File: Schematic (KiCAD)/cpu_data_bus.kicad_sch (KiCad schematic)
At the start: 144 parts, among them P13 INVERT, P19 INVERT, P26 INVERT, P5 INVERT, P7 INVERT, X18 INVERT, X19 INVERT, X20 INVERT, X21 INVERT, X22 INVERT, X23 INVERT, X24 INVERT, X25 INVERT, Y11 INVERT, Y12 INVERT, Y18 INVERT, Y19 INVERT, Y25 INVERT, Y26 INVERT, Y4 INVERT, Y5 INVERT

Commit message: - Started work on the pulse channels.  - Solved at least 2 of the red traces in the SVG.  - Finally realized that "Unknown 4to1" cells are actually just ordinary And-Or-Invert "AOI22" cells.
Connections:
- net at BK47. (X): now also BK46. (X); no longer BL50. (X)
- net at BK51. (X): now also BK49. (X); no longer BK52. (X)
- new net: BK55. (X), BK56. (X), BK61. (X), BK62. (X), BK67. (X), BK68. (X), BK73. (X), BK74. (X), BL58. (X)
- new net: BK55. (X), BK56. (X), BK61. (X), BK62. (X), BK67. (X), BK68. (X), BK73. (X), BK74. (X), BL59. (X)
- new net: BK66. (X), BK67. (X)
- new net: BK53. (X), BK58. (X), BK59. (X), BK64. (X), BK65. (X), BK70. (X), BK71. (X), BK76. (X), BL61. (X)
- new net: BK63. (X), BK64. (X)
- new net: BK69. (X), BK70. (X)
- new net: BK68. (X), BK69. (X)
- new net: BK65. (X), BK66. (X)
- new net: BK57. (X), BK58. (X)
- new net: G15. (X), G16. (X)
- new net: BK75. (X), BK76. (X)
- new net: G10. (X), G9. (X)
- new net: AE13. (X), AE19. (X), G13. (X), MUL20. (X), X19. (X)
- new net: BK47. (X), BL50. (X)
- new net: G1. (X), G2. (X)
- new net: G7. (X), G8. (X)
- new net: G11. (X), G12. (X)
- new net: G5. (X), G6. (X)
- new net: BK53. (X), BK54. (X)
- new net: G3. (X), G4. (X)
- new net: BK48. (X), BP2. (X)
- new net: BP2. (X), BP3. (X)
- new net: BK55. (X), BK73. (X), BK74. (X), BL60. (X)
- new net: BK54. (X), BK55. (X)
- new net: BK72. (X), BK73. (X)
- new net: BK71. (X), BK72. (X)
- new net: BK74. (X), BK75. (X)
- new net: BK74. (X), BL57. (X)
- new net: B26. (X), B27. (X)
- new net: BK60. (X), BK61. (X)
- new net: BK59. (X), BK60. (X)
- new net: BK56. (X), BK57. (X)
- new net: BK62. (X), BK63. (X)
- new net: BK51. (X), BK52. (X)
- new net: BP1. (X), BP2. (X)
- new net: BK50. (X), BK51. (X)
- new net: BK46. (X), BK51. (X)
- new net: BP2. (X), BP4. (X)
- new net: BK45. (X), BK46. (X)

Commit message: - Pulse DAC logic is now complete.  - The 4-bit adders are verified correct using Excel.    - This revealed 1 tracing error and also 3 XNOR gates that are actually XOR in this case.  - Now including a PDF version of the schematic.
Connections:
- net at BK47. (X): now also BK46. (X); no longer BL50. (X)
- net at BK51. (X): now also BK49. (X); no longer BK52. (X)
- new net: BK55. (X), BK56. (X), BK61. (X), BK62. (X), BK67. (X), BK68. (X), BK73. (X), BK74. (X), BL58. (X)
- new net: BK55. (X), BK56. (X), BK61. (X), BK62. (X), BK67. (X), BK68. (X), BK73. (X), BK74. (X), BL59. (X)
- new net: BK66. (X), BK67. (X)
- new net: BK53. (X), BK58. (X), BK59. (X), BK64. (X), BK65. (X), BK70. (X), BK71. (X), BK76. (X), BL61. (X)
- new net: BK63. (X), BK64. (X)
- new net: BK69. (X), BK70. (X)
- new net: BK68. (X), BK69. (X)
- new net: BK65. (X), BK66. (X)
- new net: BK57. (X), BK58. (X)
- new net: G15. (X), G16. (X)
- new net: BK75. (X), BK76. (X)
- new net: G10. (X), G9. (X)
- new net: AE13. (X), AE19. (X), G13. (X), MUL20. (X), X19. (X)
- new net: BK47. (X), BL50. (X)
- new net: G1. (X), G2. (X)
- new net: G7. (X), G8. (X)
- new net: G11. (X), G12. (X)
- new net: G5. (X), G6. (X)
- new net: BK53. (X), BK54. (X)
- new net: G3. (X), G4. (X)
- new net: BK48. (X), BP2. (X)
- new net: BP2. (X), BP3. (X)
- new net: BK55. (X), BK73. (X), BK74. (X), BL60. (X)
- new net: BK54. (X), BK55. (X)
- new net: BK72. (X), BK73. (X)
- new net: BK71. (X), BK72. (X)
- new net: BK74. (X), BK75. (X)
- new net: BK74. (X), BL57. (X)
- new net: B26. (X), B27. (X)
- new net: BK60. (X), BK61. (X)
- new net: BK59. (X), BK60. (X)
- new net: BK56. (X), BK57. (X)
- new net: BK62. (X), BK63. (X)
- new net: BK51. (X), BK52. (X)
- new net: BP1. (X), BP2. (X)
- new net: BK50. (X), BK51. (X)
- new net: BK46. (X), BK51. (X)
- new net: BP2. (X), BP4. (X)
- new net: BK45. (X), BK46. (X)

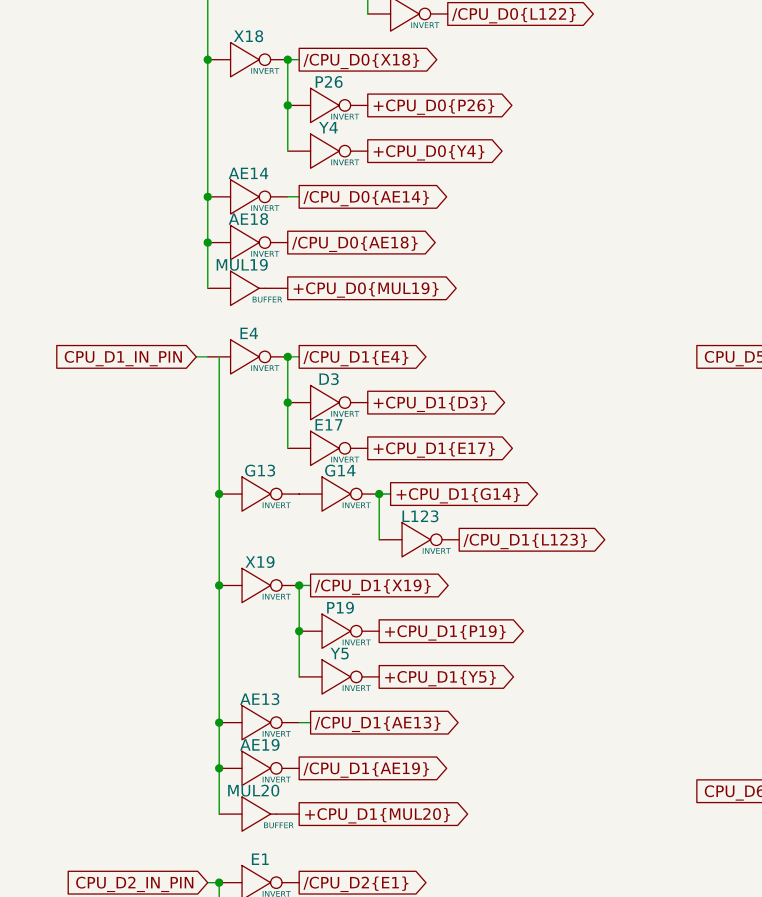
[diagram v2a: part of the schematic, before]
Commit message: Schematic Updates:  - Added all 10-bit CHR banking registers $5120 - $512B, including where all 10 bits come from when written.  - Added 8-bit CHR bank register $5202, which is the bank used when rendering the V-Split region.    + V-Split seems to always be 8-bit, 8kB bank regardless of CHR mode.  The wiki doesn't say that and I don't know for sure.  - Added decoding logic that activates the correct CHR bank for CHR A10, A11, A12 (corresponding to columns AV, AW, AX).  - Noted, AX15 activates $5202 CHR Bank for V-Split region.  AX16 activates CHR Bank from data stored in ExRAM for extended attributes.  Therefore, AX15 driven by AT1 High means we specifically are in v-split region, and not extended attribute mode.  With this knowledge, backtracking up the chain from AT1 to N14 sheds very useful insight what the 3-bit shift register at N11/N12/N13 is doing.  We now know that N14 goes low specifically for pattern table fetches when rendering the V-split region, and does not appear dual-purposed for extended attribute fetch sequencing.  This may seem rather subtle or unimportant, but it is a good advancement for higher level understanding what that mysterious shift register might be doing.
SVG Trace Updates:
 - Registers $5120, 5121, 5122, 5123 (first 4 CHR bank register), the outputs were labeled in reverse order.
 - Register $5130 (highest CHR bank bits), the outputs were labeled with backwards polarity.  The error was not having taken into account that the CPU data bus input to the latches came already inverted to begin with.
 - Still wrong: Cell AV7, 2-input NAND gate.  One of the inputs is missing and it logically should be driven by AS19 like the 4 cells to its direct right.  I can't quite make out how it makes that connection.
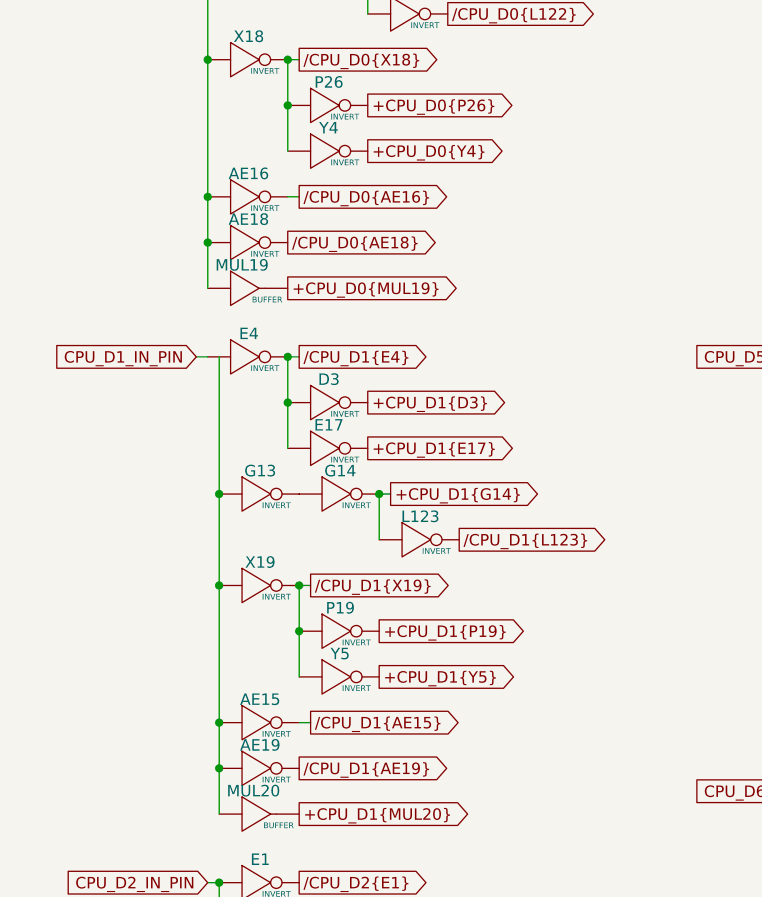
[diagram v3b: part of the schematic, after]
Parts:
- renumbered AE13 to AE15, AE14 to AE16
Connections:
- net at BK47. (X): now also BK46. (X); no longer BL50. (X)
- net at BK51. (X): now also BK49. (X); no longer BK52. (X)
- net /CPU_D0{AE14} renamed /CPU_D0{AE16}
- net /CPU_D1{AE13} renamed /CPU_D1{AE15}
- new net: BK55. (X), BK56. (X), BK61. (X), BK62. (X), BK67. (X), BK68. (X), BK73. (X), BK74. (X), BL58. (X)
- new net: BK55. (X), BK56. (X), BK61. (X), BK62. (X), BK67. (X), BK68. (X), BK73. (X), BK74. (X), BL59. (X)
- new net: BK66. (X), BK67. (X)
- new net: BK53. (X), BK58. (X), BK59. (X), BK64. (X), BK65. (X), BK70. (X), BK71. (X), BK76. (X), BL61. (X)
- new net: BK63. (X), BK64. (X)
- new net: BK69. (X), BK70. (X)
- new net: BK68. (X), BK69. (X)
- new net: BK65. (X), BK66. (X)
- new net: BK57. (X), BK58. (X)
- new net: G15. (X), G16. (X)
- new net: BK75. (X), BK76. (X)
- new net: G10. (X), G9. (X)
- new net: AE15. (X), AE19. (X), G13. (X), MUL20. (X), X19. (X)
- new net: BK47. (X), BL50. (X)
- new net: G1. (X), G2. (X)
- new net: G7. (X), G8. (X)
- new net: G11. (X), G12. (X)
- new net: G5. (X), G6. (X)
- new net: BK53. (X), BK54. (X)
- new net: G3. (X), G4. (X)
- new net: BK48. (X), BP2. (X)
- new net: BP2. (X), BP3. (X)
- new net: BK55. (X), BK73. (X), BK74. (X), BL60. (X)
- new net: BK54. (X), BK55. (X)
- new net: BK72. (X), BK73. (X)
- new net: BK71. (X), BK72. (X)
- new net: BK74. (X), BK75. (X)
- new net: BK74. (X), BL57. (X)
- new net: B26. (X), B27. (X)
- new net: BK60. (X), BK61. (X)
- new net: BK59. (X), BK60. (X)
- new net: BK56. (X), BK57. (X)
- new net: BK62. (X), BK63. (X)
- new net: BK51. (X), BK52. (X)
- new net: BP1. (X), BP2. (X)
- new net: BK50. (X), BK51. (X)
- new net: BK46. (X), BK51. (X)
- new net: BP2. (X), BP4. (X)
- new net: BK45. (X), BK46. (X)
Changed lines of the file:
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@@
 		)
 	)
-	(global_label "{slash}CPU_D1{AE13}"
+	(global_label "{slash}CPU_D1{AE15}"
 		(shape output)
 		(at 44.45 125.73 0)
@@
 		)
 	)
-	(global_label "{slash}CPU_D0{AE14}"
+	(global_label "{slash}CPU_D0{AE16}"
 		(shape output)
 		(at 43.18 67.31 0)
@@
 		(dnp no)
 		(fields_autoplaced yes)
-		(property "Reference" "AE13"
+		(property "Reference" "AE15"
 			(at 38.862 122.428 0)
 			(do_not_autoplace yes)
@@
 			(project ""
 				(path "/46093bf6-f83e-4237-9ece-7350a682aff0/f8de81e6-db49-4c78-bf33-f3fdf7c2f2f8"
-					(reference "AE13")
+					(reference "AE15")
 					(unit 1)
 				)
@@
 		(dnp no)
 		(fields_autoplaced yes)
-		(property "Reference" "AE14"
+		(property "Reference" "AE16"
 			(at 37.592 64.008 0)
 			(do_not_autoplace yes)
@@
 			(project ""
 				(path "/46093bf6-f83e-4237-9ece-7350a682aff0/f8de81e6-db49-4c78-bf33-f3fdf7c2f2f8"
-					(reference "AE14")
+					(reference "AE16")
 					(unit 1)
 				)

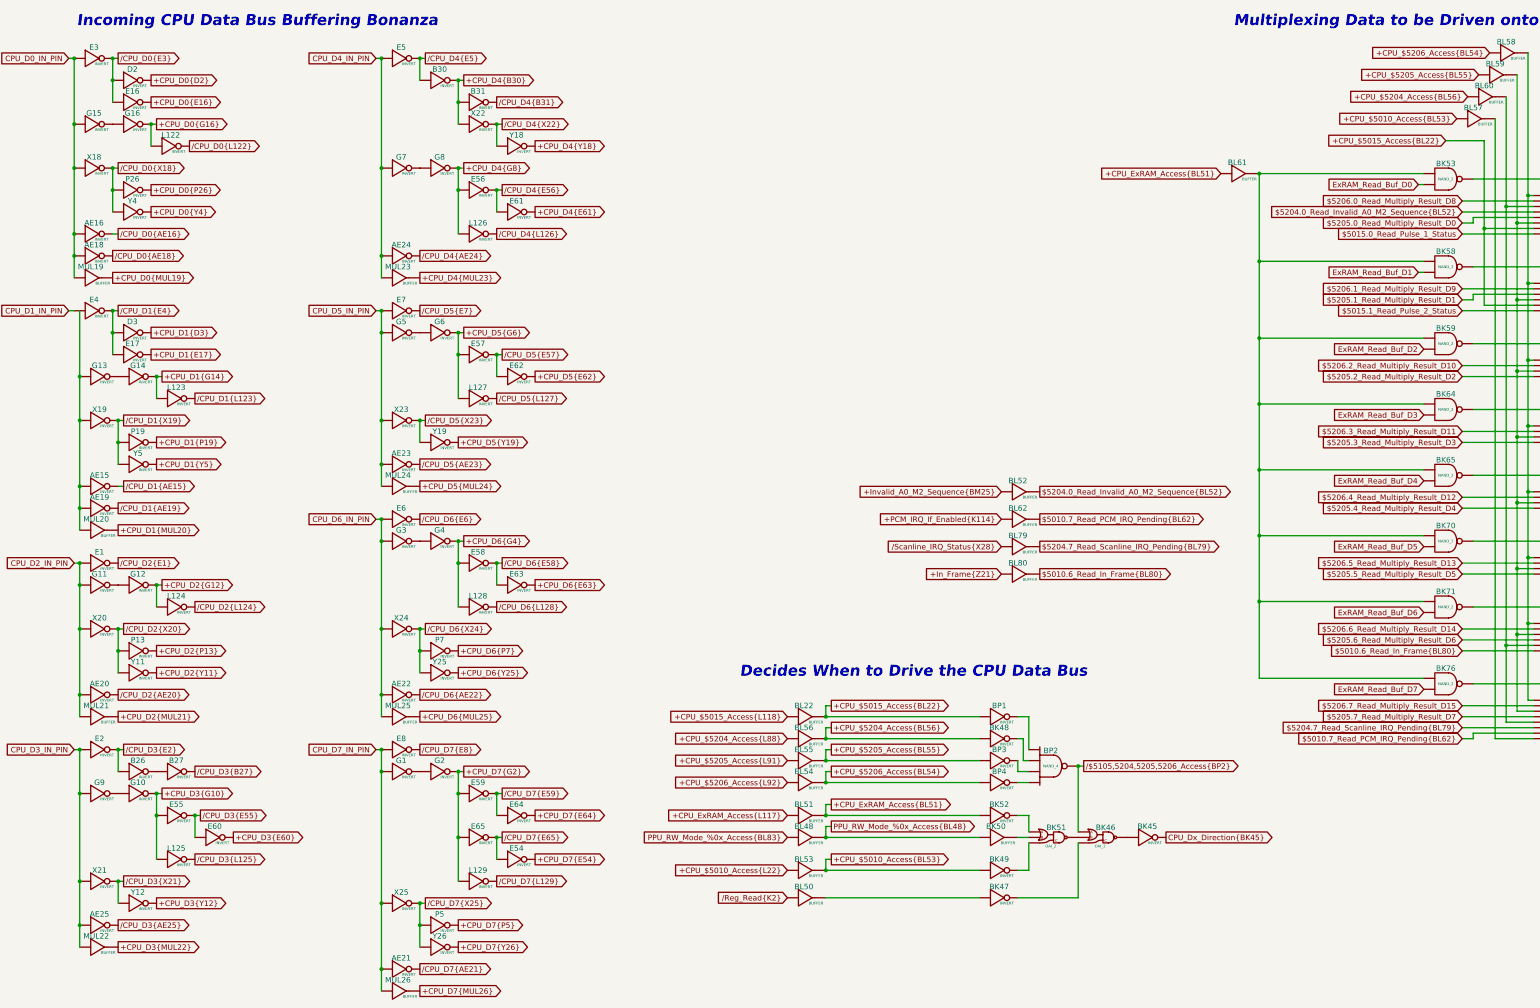
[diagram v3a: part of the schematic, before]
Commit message: - All cells in the left and center areas have now been added into the schematics.  - Changed naming of the PDF files; I was accidentally writing over furrtek's original with my new PDF.
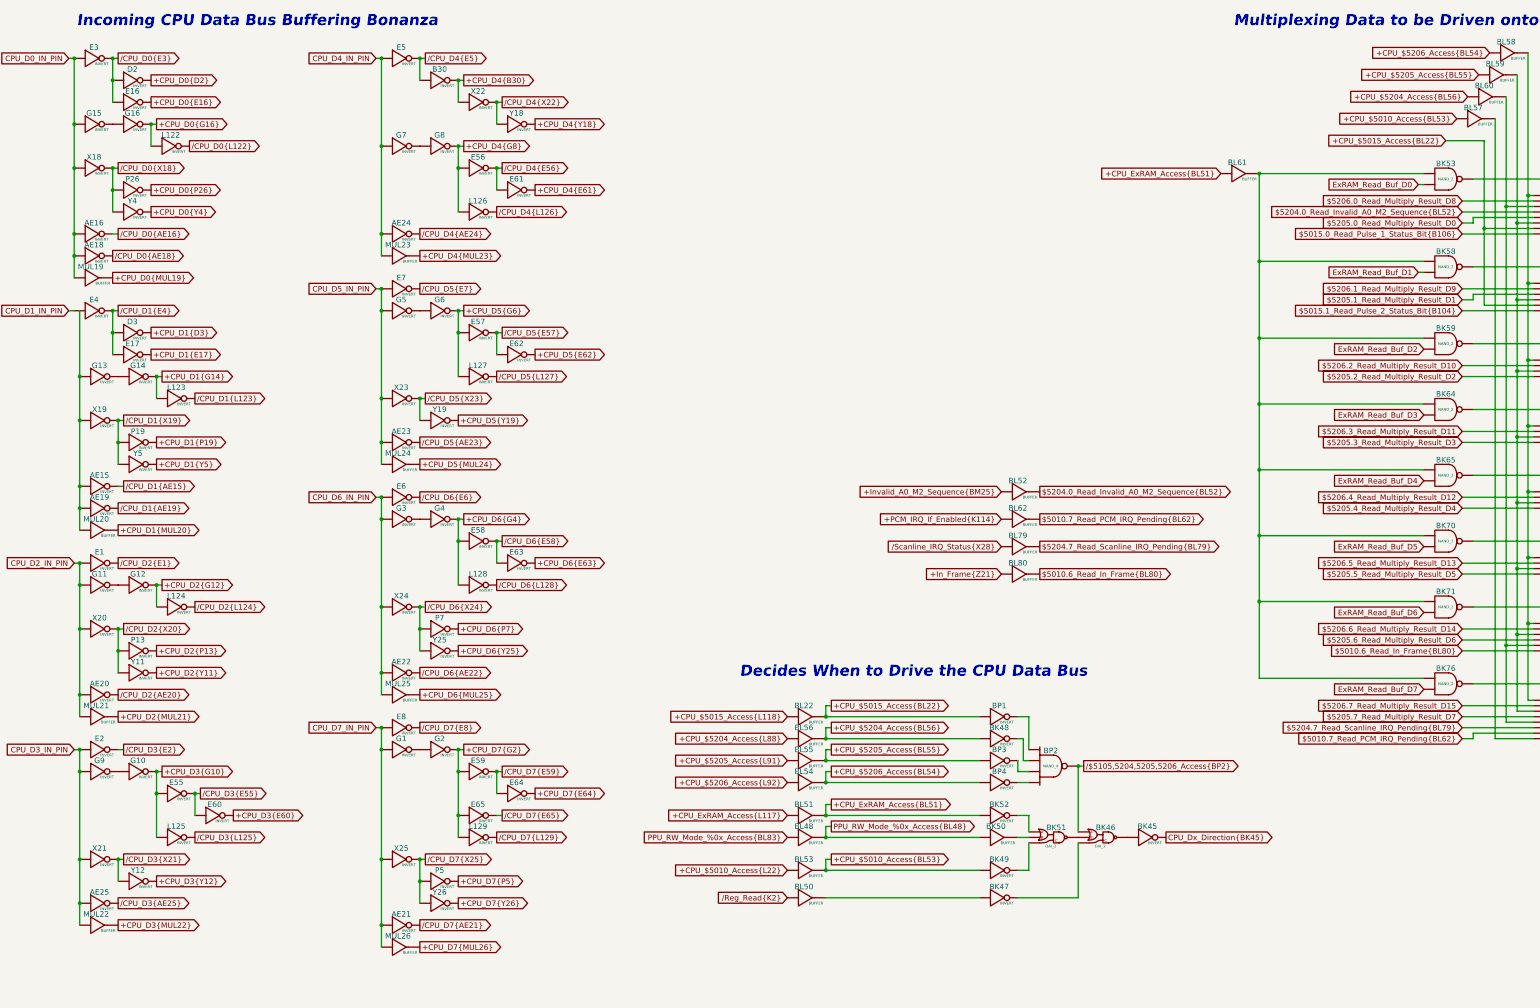
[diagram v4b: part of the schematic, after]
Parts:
- removed B26, B27, B31, E54: INVERT, symbol MMC5:INVERT
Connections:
- net $5015.0_Read_Pulse_1_Status is gone; now on net +CPU_$5015_Access{BL22}: BK55. (X)
- net $5015.1_Read_Pulse_2_Status is gone; now on net +CPU_$5015_Access{BL22}: BK56. (X)
- net at BK47. (X): now also BK46. (X); no longer BL50. (X)
- net at BK51. (X): now also BK49. (X); no longer BK52. (X)
- new net: BK55. (X), BK56. (X), BK61. (X), BK62. (X), BK67. (X), BK68. (X), BK73. (X), BK74. (X), BL58. (X)
- new net: BK55. (X), BK56. (X), BK61. (X), BK62. (X), BK67. (X), BK68. (X), BK73. (X), BK74. (X), BL59. (X)
- new net: BK66. (X), BK67. (X)
- new net: BK53. (X), BK58. (X), BK59. (X), BK64. (X), BK65. (X), BK70. (X), BK71. (X), BK76. (X), BL61. (X)
- new net: BK63. (X), BK64. (X)
- new net: BK69. (X), BK70. (X)
- new net: BK68. (X), BK69. (X)
- new net: BK65. (X), BK66. (X)
- new net: BK57. (X), BK58. (X)
- new net: G15. (X), G16. (X)
- new net: BK75. (X), BK76. (X)
- new net: G10. (X), G9. (X)
- new net: AE15. (X), AE19. (X), G13. (X), MUL20. (X), X19. (X)
- new net: BK47. (X), BL50. (X)
- new net: G1. (X), G2. (X)
- new net: G7. (X), G8. (X)
- new net: G11. (X), G12. (X)
- new net: G5. (X), G6. (X)
- new net: BK53. (X), BK54. (X)
- new net: G3. (X), G4. (X)
- new net: BK48. (X), BP2. (X)
- new net: BP2. (X), BP3. (X)
- new net: BK55. (X), BK73. (X), BK74. (X), BL60. (X)
- new net: BK54. (X), BK55. (X)
- new net: BK72. (X), BK73. (X)
- new net: BK71. (X), BK72. (X)
- new net: BK74. (X), BK75. (X)
- new net: BK74. (X), BL57. (X)
- new net: BK60. (X), BK61. (X)
- new net: BK59. (X), BK60. (X)
- new net: BK56. (X), BK57. (X)
- new net: BK62. (X), BK63. (X)
- new net: BK51. (X), BK52. (X)
- new net: BP1. (X), BP2. (X)
- new net: BK50. (X), BK51. (X)
- new net: BK46. (X), BK51. (X)
- new net: BP2. (X), BP4. (X)
- new net: BK45. (X), BK46. (X)
- new net $5015.0_Read_Pulse_1_Status_Bit{B106}: BK55. (X)
- new net $5015.1_Read_Pulse_2_Status_Bit{B104}: BK56. (X)
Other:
- moved on the sheet: AE21, AE22, AE23, AE24, AE25, E55, E56, E57, E58, E59, E6, E60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
